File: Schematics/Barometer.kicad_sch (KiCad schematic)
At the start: 4 parts, among them U4 MPL3115A2R1

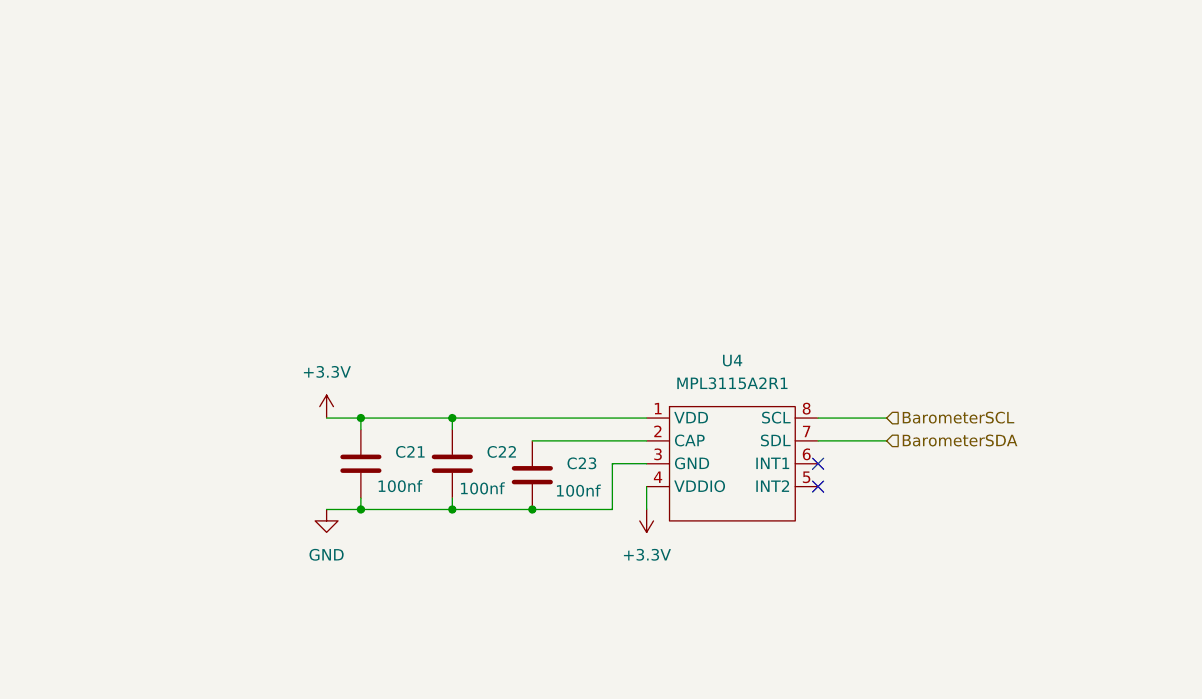
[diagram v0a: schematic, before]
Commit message: started new design with esp32
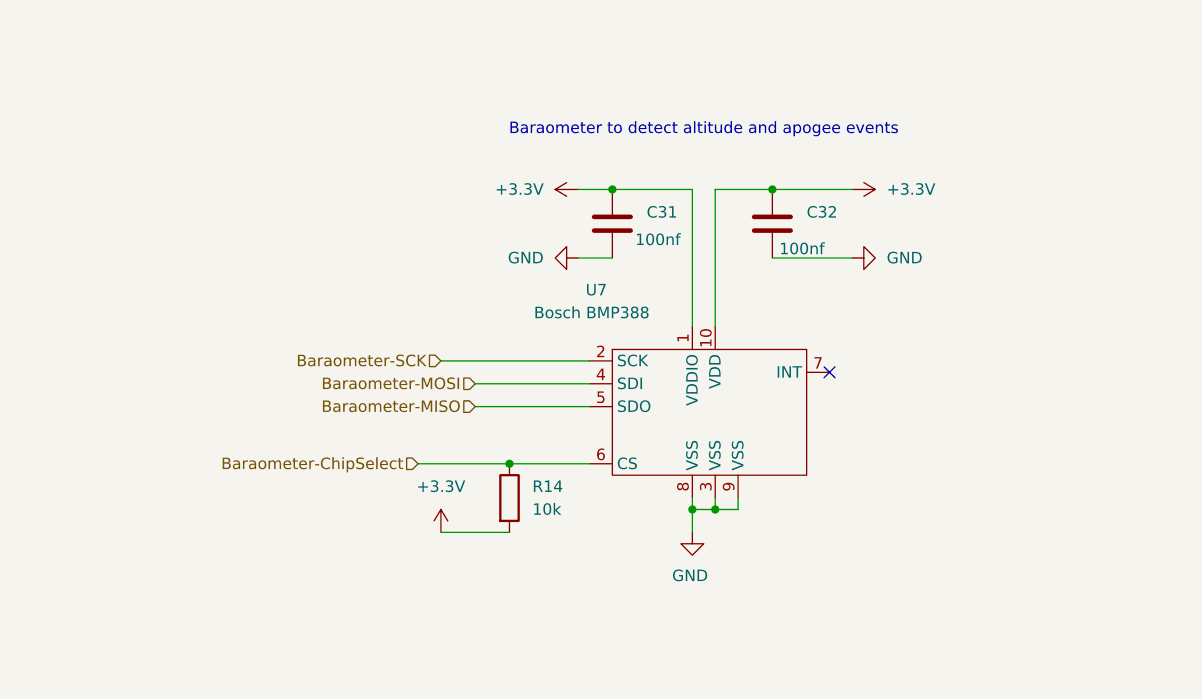
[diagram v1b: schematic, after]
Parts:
- removed C21, C22, C23: 100nf, Capacitor_SMD:C_0805_2012Metric_Pad1.18x1.45mm_HandSolder, symbol Device:C
- removed U4: MPL3115A2R1, myFootprints:PSON80P300X300X100-8N, symbol Footprints:MPL3115A2R1
- added C31, C32: 100nf, Capacitor_SMD:C_0805_2012Metric_Pad1.18x1.45mm_HandSolder, symbol Device:C
- added R14: 10k, Resistor_SMD:R_0805_2012Metric_Pad1.20x1.40mm_HandSolder, symbol Device:R
- added U7: Bosch BMP388, myFootprints:PQFN50P200X200X80-10N, symbol Footprints:MPL3115A2R1
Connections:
- net +3.3V: now also C31.1, C32.1, R14.2, U7.1 (VDDIO), U7.10 (VDD)
- net GND: now also C31.2, C32.2, U7.3 (VSS), U7.8 (VSS), U7.9 (VSS)
- new net Baraometer-ChipSelect: R14.1, U7.6 (CS)
- new net Baraometer-MISO: U7.5 (SDO)
- new net Baraometer-MOSI: U7.4 (SDI)
- new net Baraometer-SCK: U7.2 (SCK)
- no-connect marks 2 -> 1
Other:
- note added: "Baraometer to detect altitude and apogee events"

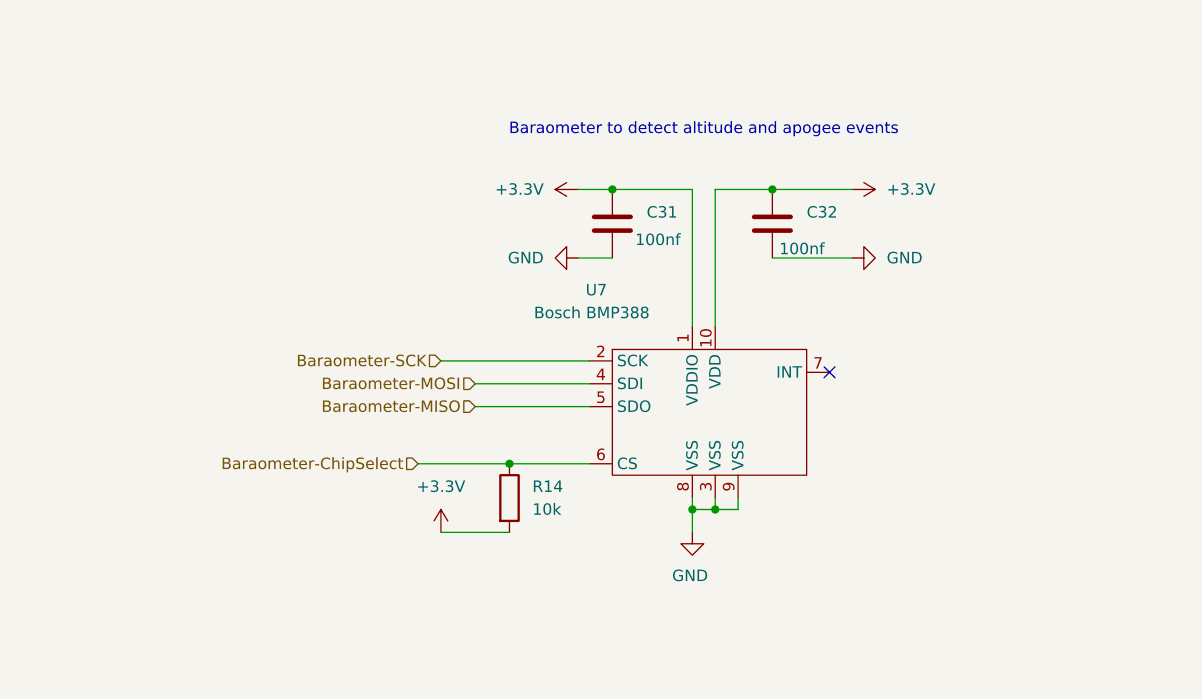
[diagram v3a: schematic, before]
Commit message: Added encoder connection for parafoil motor position information, in buy order ready for purchase
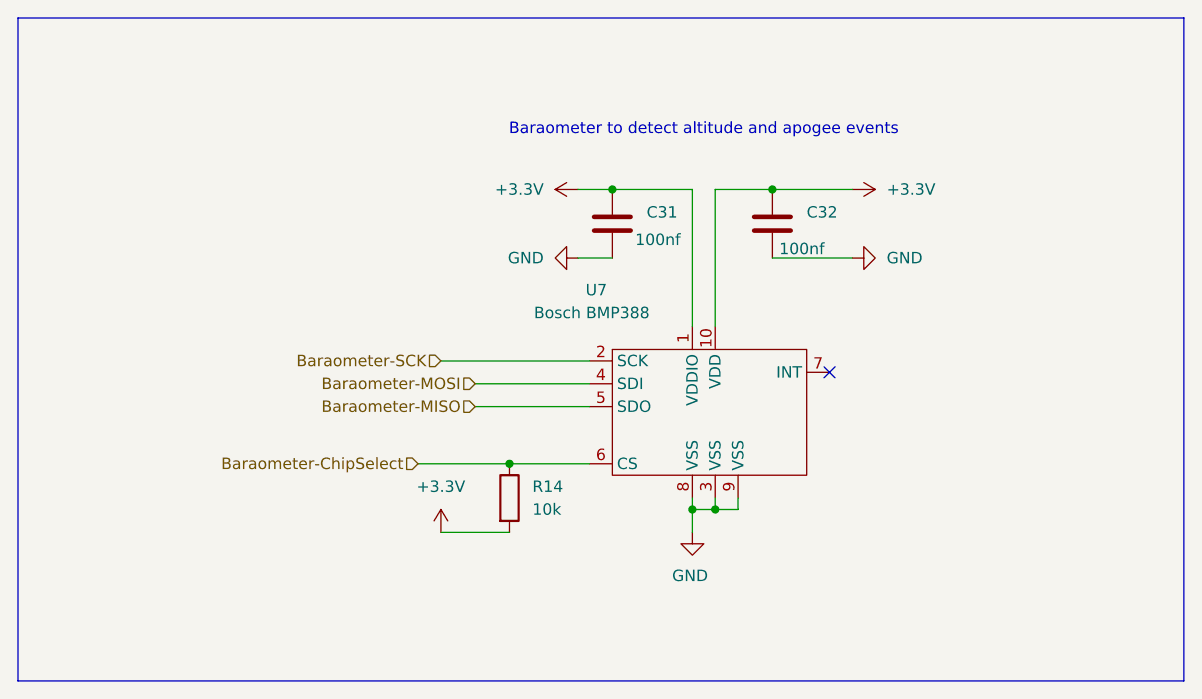
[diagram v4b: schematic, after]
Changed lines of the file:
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@@
 	(generator_version "10.0")
 	(paper "A4")
+	(rectangle
+		(start 73.66 54.61)
+		(end 203.2 128.27)
+		(stroke
+			(width 0)
+			(type default)
+		)
+		(fill
+			(type none)
+		)
+	)
 	(text "Baraometer to detect altitude and apogee events"
 		(exclude_from_sim no)
